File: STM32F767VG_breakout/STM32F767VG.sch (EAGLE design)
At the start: 43 parts, among them IC1 STM32F767VGT6, IC3 LD117AS33TR, X4 8MHz, X5 32.768kHz, X6 MSTBA2

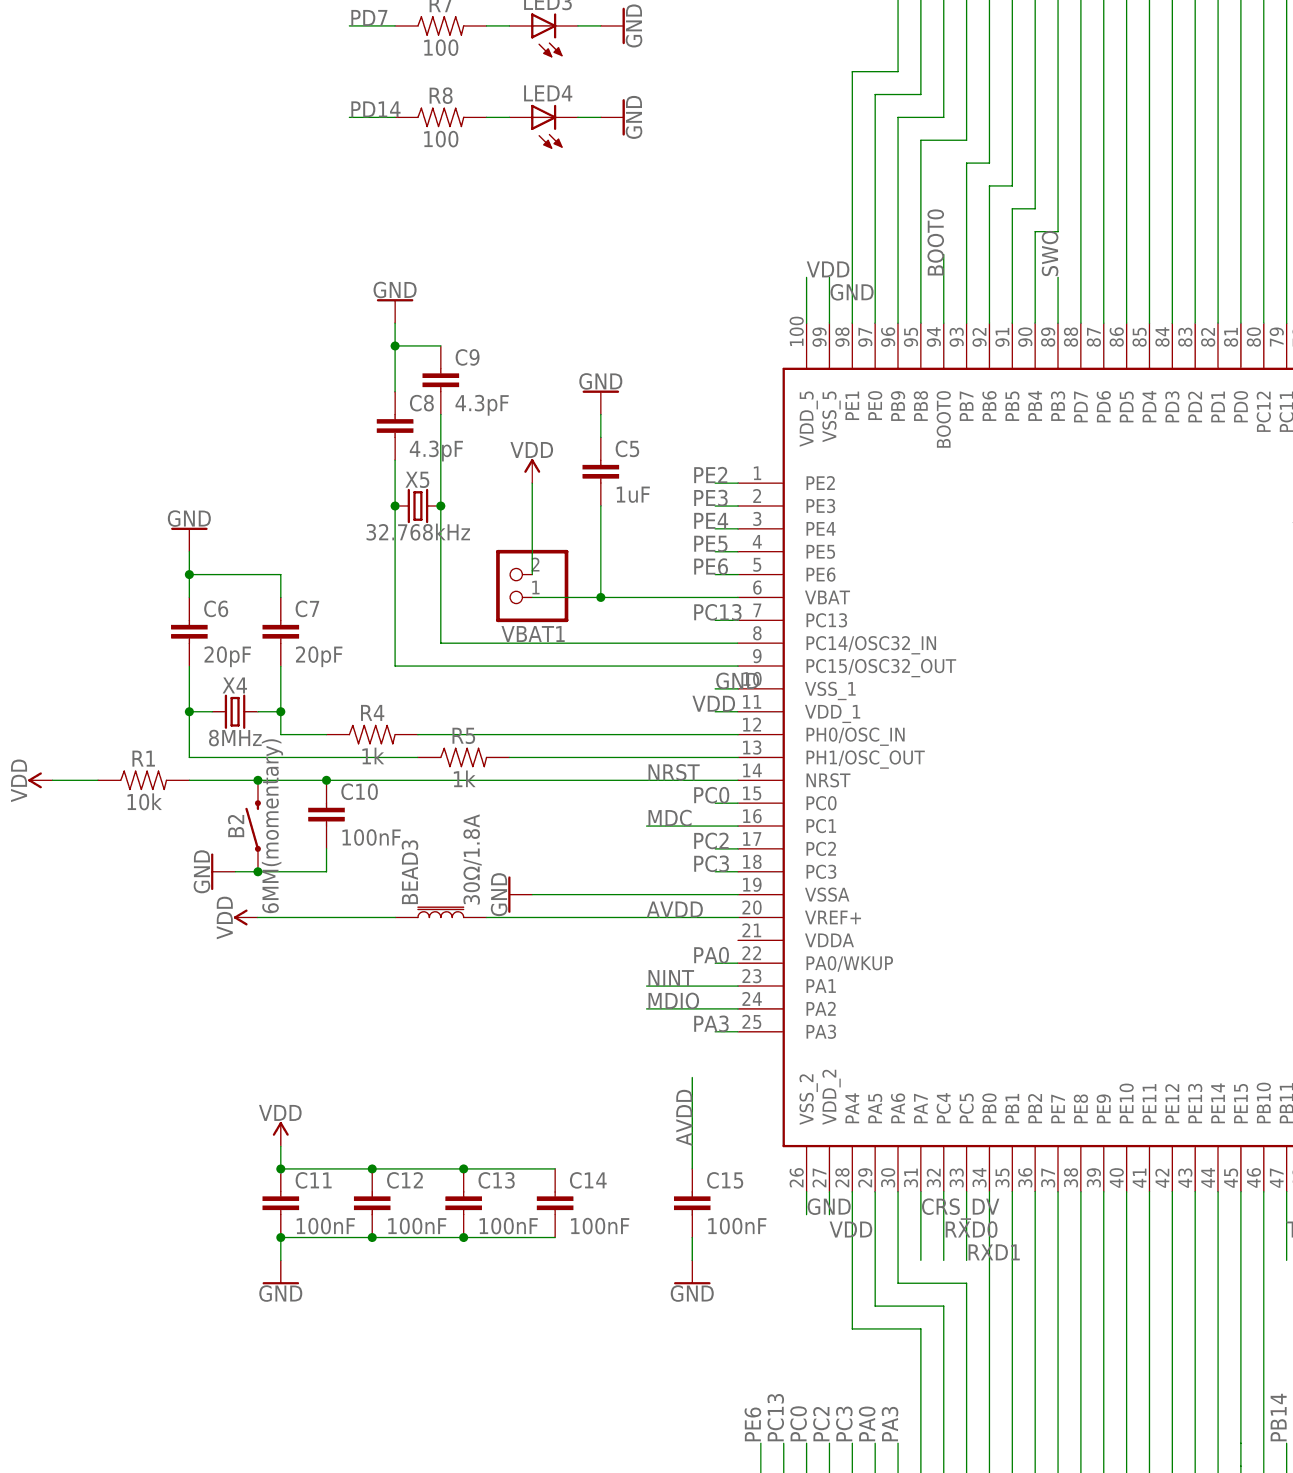
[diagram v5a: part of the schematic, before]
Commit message: Iniitial Progress on designing PCB
Organized the components onto the design space. Put the pairing capacitors near the VCC and VSS pins as suggested in meeting.
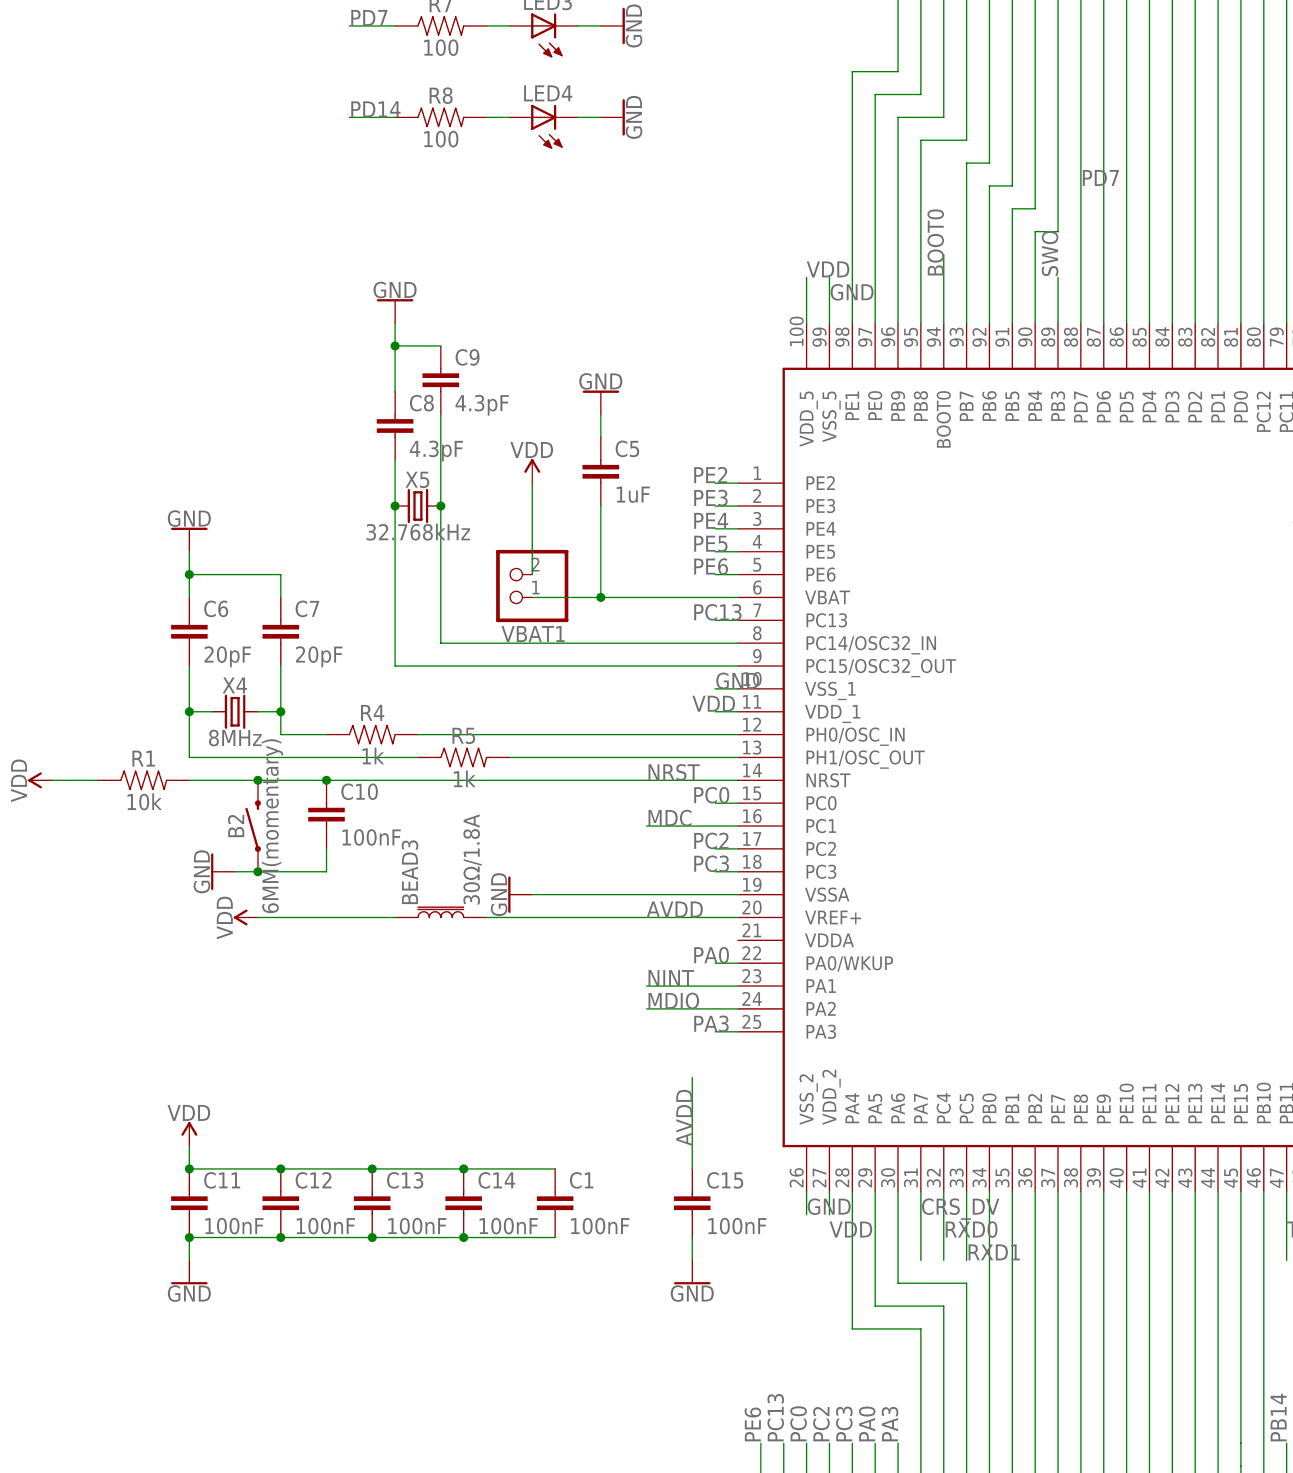
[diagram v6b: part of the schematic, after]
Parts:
- added C1: 100nF, ee2parts:C2.5P
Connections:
- removed net N$39: IC1.PD7, JP2.13
- net GND: now also C1.2
- net PD7: now also IC1.PD7, JP2.13
- net VDD: now also C1.1
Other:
- moved on the sheet: C11, C12, C13, C14
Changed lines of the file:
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@@
 <part name="R8" library="SparkFun-Resistors" deviceset="10KOHM" device="-HORIZ-1/4W-1%" value="100"/>
 <part name="GND4" library="SparkFun-PowerSymbols" deviceset="GND" device=""/>
+<part name="C1" library="ee2parts" deviceset="C" device="2.5P" value="100nF"/>
 </parts>
 <sheets>
@@
 <instance part="BEAD3" gate="G$1" x="-33.02" y="-48.26" rot="R90"/>
 <instance part="C10" gate="G$1" x="-45.72" y="-38.1"/>
-<instance part="C11" gate="G$1" x="-50.8" y="-81.28"/>
-<instance part="C12" gate="G$1" x="-40.64" y="-81.28"/>
-<instance part="C13" gate="G$1" x="-30.48" y="-81.28"/>
-<instance part="C14" gate="G$1" x="-20.32" y="-81.28"/>
-<instance part="SUPPLY10" gate="VDD" x="-50.8" y="-73.66"/>
+<instance part="C11" gate="G$1" x="-60.96" y="-81.28"/>
+<instance part="C12" gate="G$1" x="-50.8" y="-81.28"/>
+<instance part="C13" gate="G$1" x="-40.64" y="-81.28"/>
+<instance part="C14" gate="G$1" x="-30.48" y="-81.28"/>
+<instance part="SUPPLY10" gate="VDD" x="-60.96" y="-73.66"/>
 <instance part="JTAG1" gate="A" x="129.54" y="-48.26" rot="MR0"/>
 <instance part="SUPPLY12" gate="VDD" x="144.78" y="-40.64" rot="R270"/>
 <instance part="BT1" gate="G$1" x="129.54" y="-71.12" rot="MR0"/>
 <instance part="SUPPLY13" gate="VDD" x="147.32" y="-71.12" rot="R270"/>
-<instance part="GND30" gate="1" x="-50.8" y="-88.9"/>
+<instance part="GND30" gate="1" x="-60.96" y="-88.9"/>
 <instance part="GND31" gate="1" x="152.4" y="-45.72" rot="R90"/>
 <instance part="PWR1" gate="A" x="129.54" y="-86.36" rot="R180"/>
@@
 <instance part="R8" gate="G$1" x="-33.02" y="40.64"/>
 <instance part="GND4" gate="1" x="-12.7" y="40.64" rot="R90"/>
+<instance part="C1" gate="G$1" x="-20.32" y="-81.28"/>
 </instances>
 <busses>
@@
 <segment>
 <pinref part="C11" gate="G$1" pin="2"/>
-<wire x1="-50.8" y1="-83.82" x2="-50.8" y2="-86.36" width="0.1524" layer="91"/>
+<wire x1="-60.96" y1="-83.82" x2="-60.96" y2="-86.36" width="0.1524" layer="91"/>
 <pinref part="C12" gate="G$1" pin="2"/>
+<wire x1="-60.96" y1="-83.82" x2="-50.8" y2="-83.82" width="0.1524" layer="91"/>
+<junction x="-60.96" y="-83.82"/>
+<pinref part="C13" gate="G$1" pin="2"/>
 <wire x1="-50.8" y1="-83.82" x2="-40.64" y2="-83.82" width="0.1524" layer="91"/>
 <junction x="-50.8" y="-83.82"/>
-<pinref part="C13" gate="G$1" pin="2"/>
+<pinref part="C14" gate="G$1" pin="2"/>
 <wire x1="-40.64" y1="-83.82" x2="-30.48" y2="-83.82" width="0.1524" layer="91"/>
 <junction x="-40.64" y="-83.82"/>
-<pinref part="C14" gate="G$1" pin="2"/>
+<pinref part="GND30" gate="1" pin="GND"/>
+<pinref part="C1" gate="G$1" pin="2"/>
 <wire x1="-30.48" y1="-83.82" x2="-20.32" y2="-83.82" width="0.1524" layer="91"/>
 <junction x="-30.48" y="-83.82"/>
-<pinref part="GND30" gate="1" pin="GND"/>
 </segment>
 <segment>
@@
 <pinref part="SUPPLY10" gate="VDD" pin="VDD"/>
 <pinref part="C11" gate="G$1" pin="1"/>
-<wire x1="-50.8" y1="-73.66" x2="-50.8" y2="-76.2" width="0.1524" layer="91"/>
+<wire x1="-60.96" y1="-73.66" x2="-60.96" y2="-76.2" width="0.1524" layer="91"/>
 <pinref part="C12" gate="G$1" pin="1"/>
+<wire x1="-60.96" y1="-76.2" x2="-50.8" y2="-76.2" width="0.1524" layer="91"/>
+<junction x="-60.96" y="-76.2"/>
+<pinref part="C13" gate="G$1" pin="1"/>
 <wire x1="-50.8" y1="-76.2" x2="-40.64" y2="-76.2" width="0.1524" layer="91"/>
 <junction x="-50.8" y="-76.2"/>
-<pinref part="C13" gate="G$1" pin="1"/>
+<pinref part="C14" gate="G$1" pin="1"/>
 <wire x1="-40.64" y1="-76.2" x2="-30.48" y2="-76.2" width="0.1524" layer="91"/>
 <junction x="-40.64" y="-76.2"/>
-<pinref part="C14" gate="G$1" pin="1"/>
+<pinref part="C1" gate="G$1" pin="1"/>
 <wire x1="-30.48" y1="-76.2" x2="-20.32" y2="-76.2" width="0.1524" layer="91"/>
 <junction x="-30.48" y="-76.2"/>
@@
 </segment>
 </net>
-<net name="N$39" class="0">
-<segment>
-<pinref part="JP2" gate="A" pin="13"/>
-<pinref part="IC1" gate="G$1" pin="PD7"/>
-<wire x1="38.1" y1="68.58" x2="38.1" y2="17.78" width="0.1524" layer="91"/>
-</segment>
-</net>
 <net name="N$43" class="0">
 <segment>
@@
 <label x="-43.18" y="50.8" size="1.778" layer="95"/>
 </segment>
-</net>
+<segment>
+<pinref part="JP2" gate="A" pin="13"/>
+<pinref part="IC1" gate="G$1" pin="PD7"/>
+<wire x1="38.1" y1="68.58" x2="38.1" y2="17.78" width="0.1524" layer="91"/>
+<label x="38.1" y="33.02" size="1.778" layer="95"/>
+</segment>
+</net>

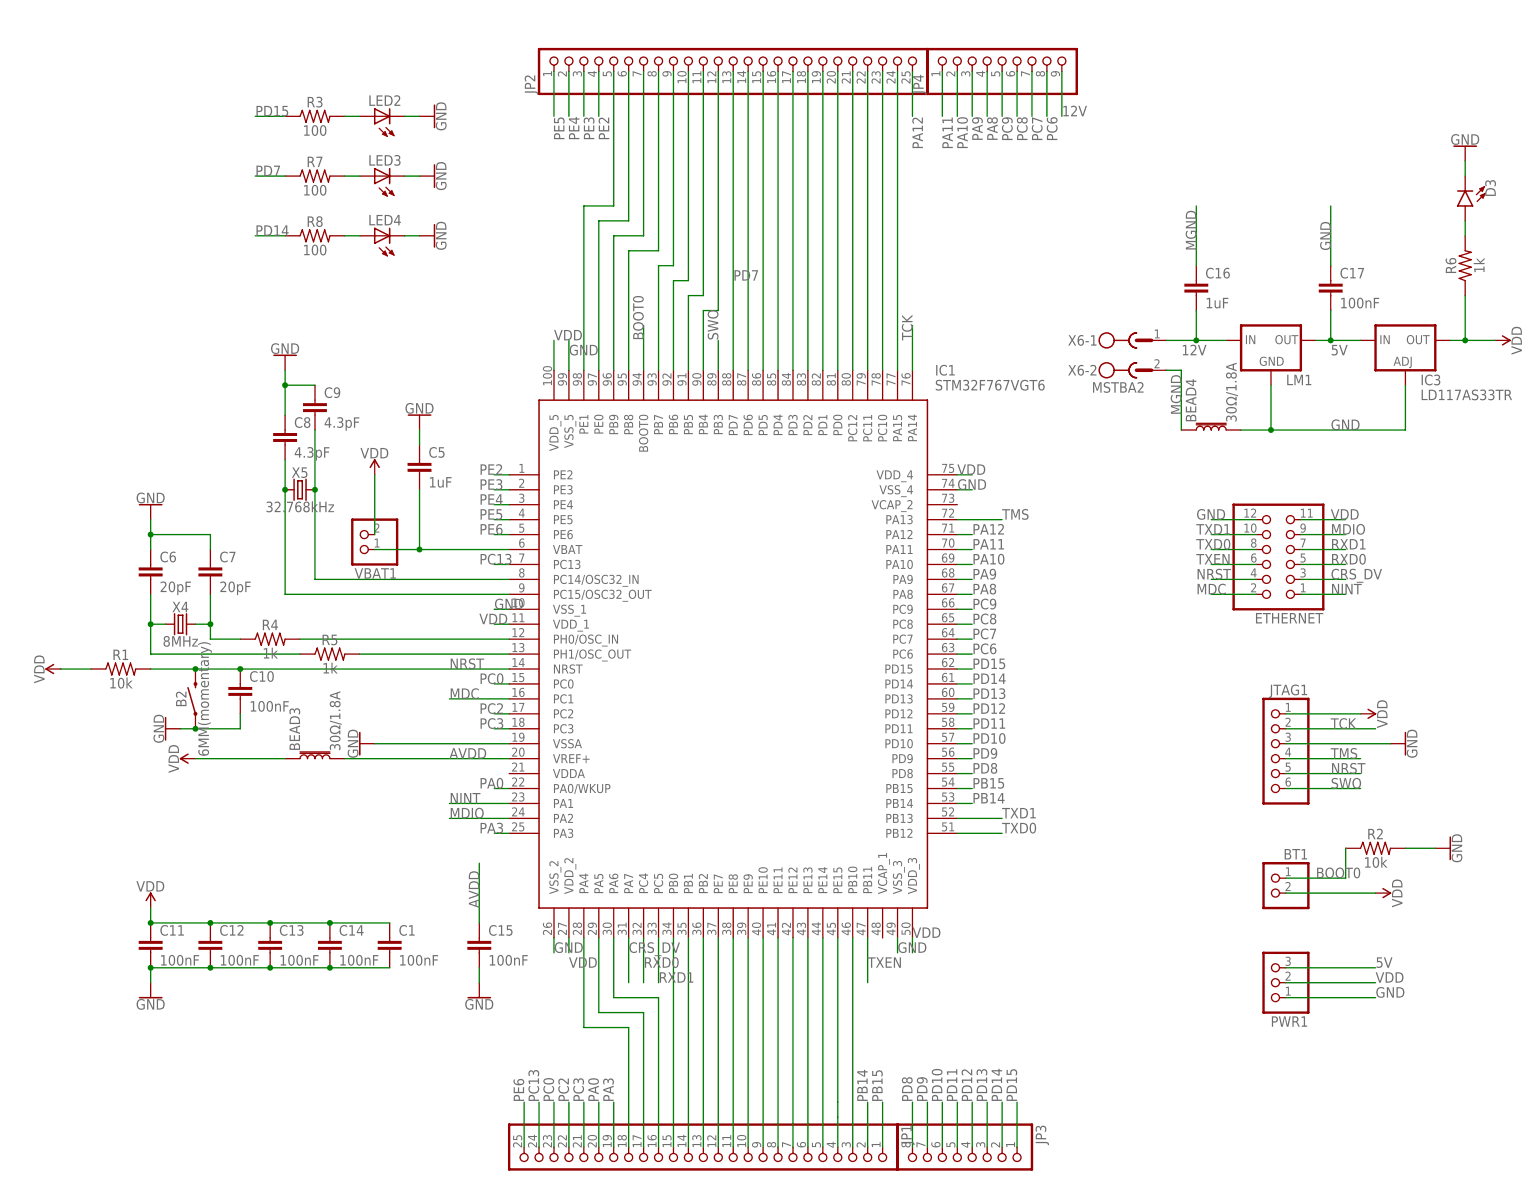
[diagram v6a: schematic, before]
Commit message: Mar 26 Feedback incorporated
Verification for correct 100nF cap package required. As per crystal datasheet, traces from crystal to microcontroller were minimized.
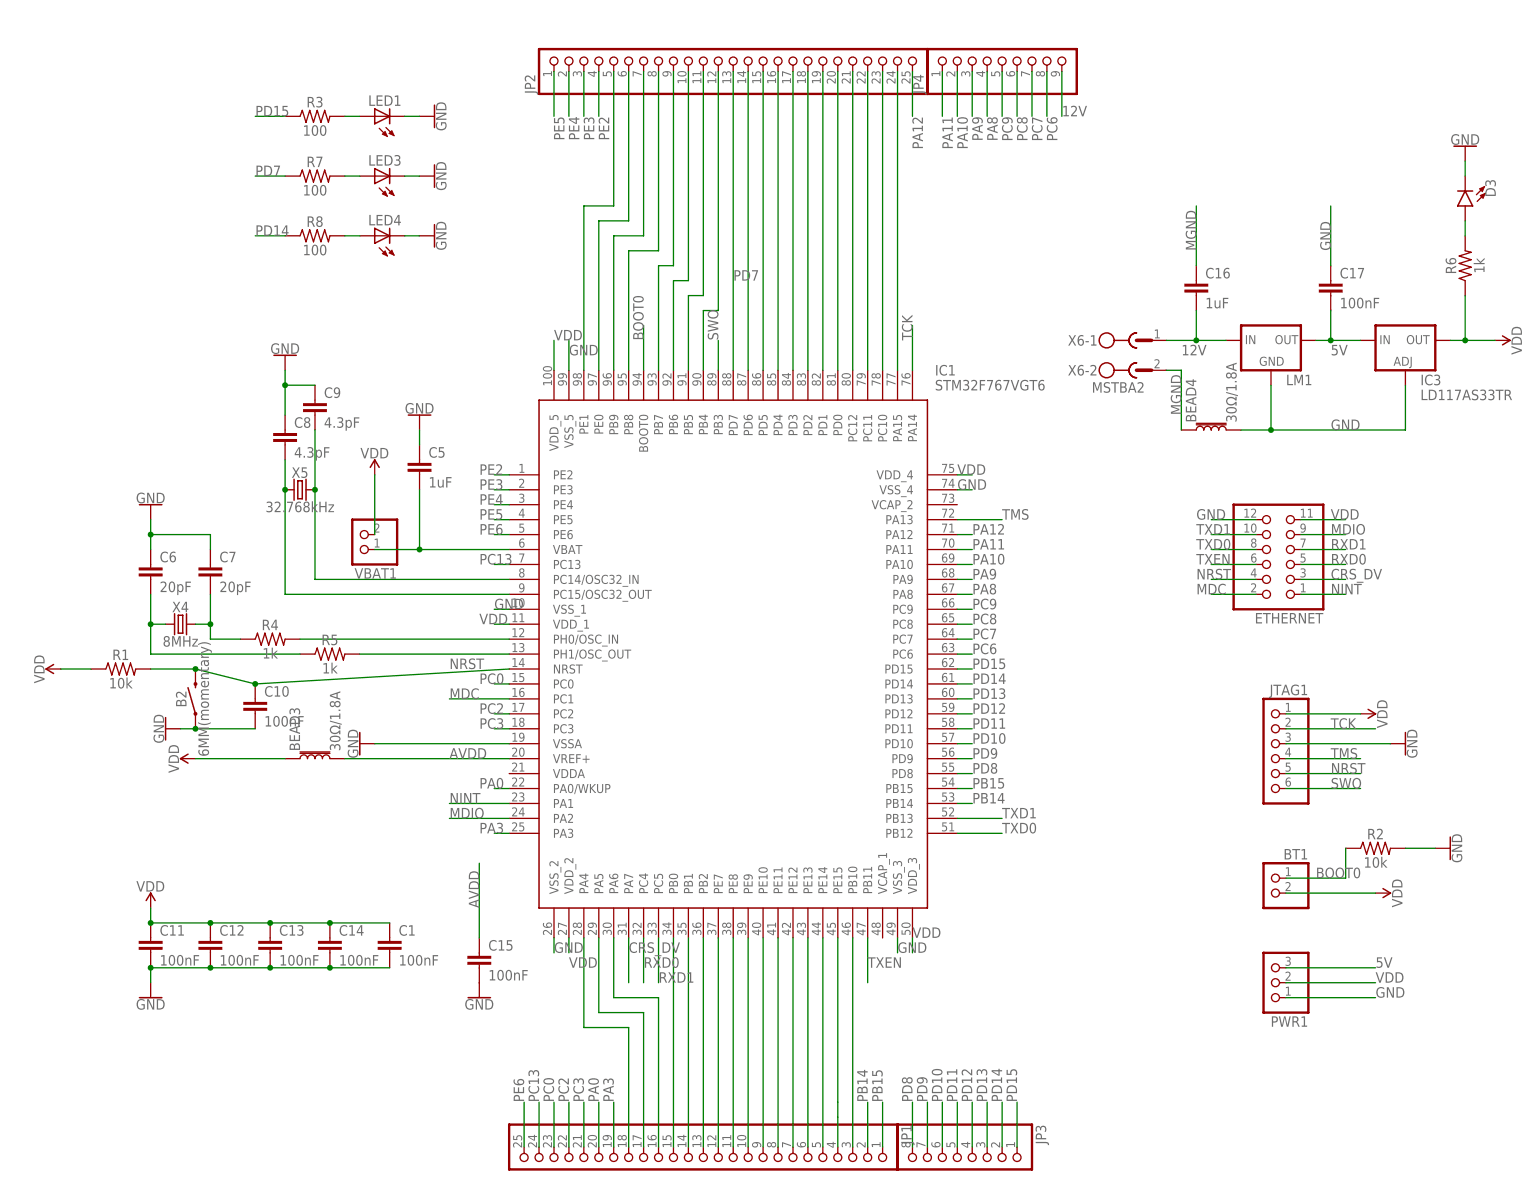
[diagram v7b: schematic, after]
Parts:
- C1, C10, C11, C12, C13, C14, C15, C17: device ee2parts:C2.5P -> eagle-ltspice:C
- renumbered LED2 to LED1
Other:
- moved on the sheet: C10, C15
